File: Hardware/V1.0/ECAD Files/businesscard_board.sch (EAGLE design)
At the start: 31 parts, among them Y1 16MHz

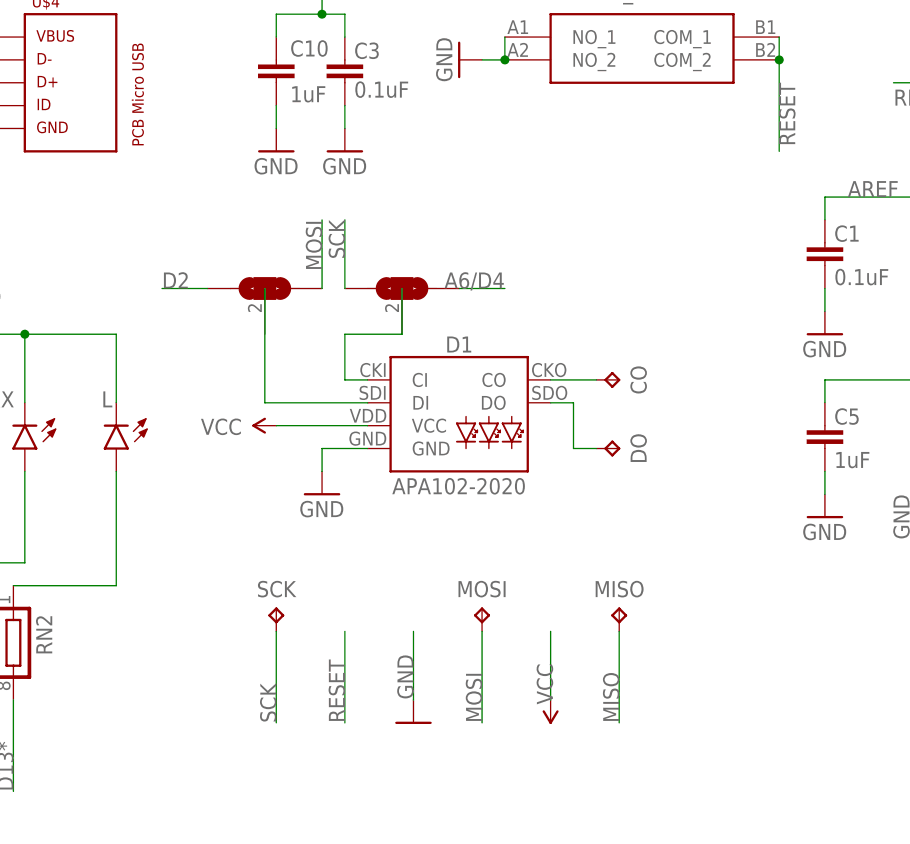
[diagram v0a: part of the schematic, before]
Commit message: Fix APA102 pinout
Fix APA102 pinout, clean up library
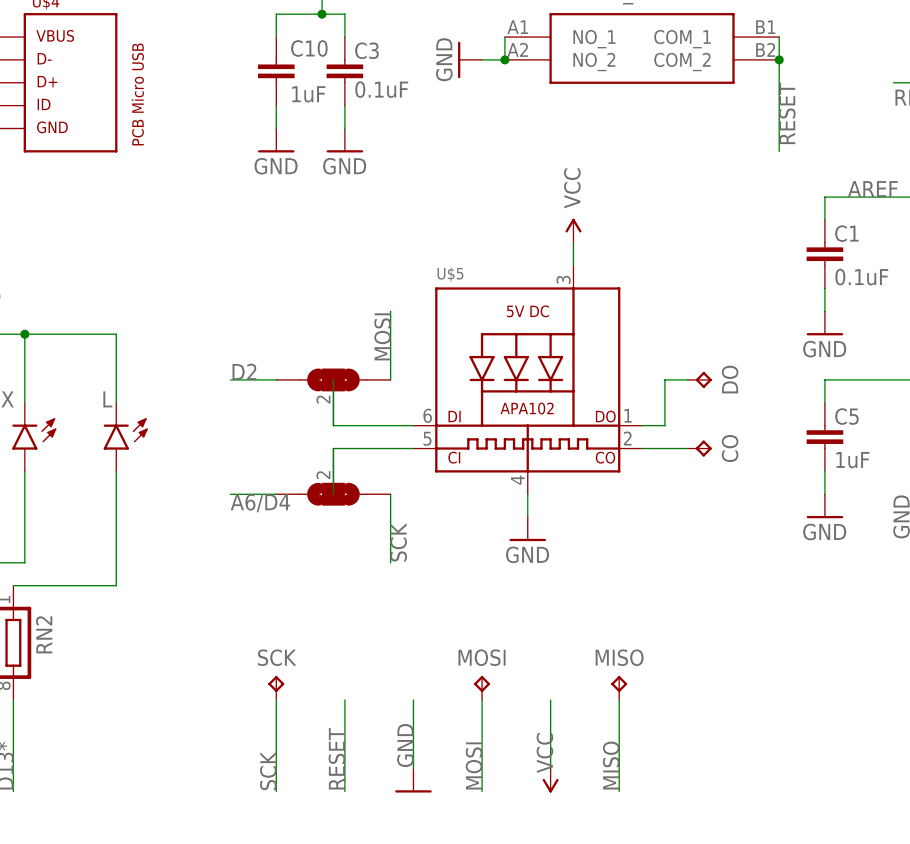
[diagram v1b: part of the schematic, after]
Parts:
- removed D1: APA102-2020, PCBusinessCard:APA102-2020
- added U$5: (no value), businesscard_board:APA1022020
- C1, C10, C2, C3, C4, C5, C6: device PCBusinessCard:CAP0603-CAP -> businesscard_board:CAP0603-CAP
- CO, DO, MISO, MOSI, SCK: device PCBusinessCard:TPTP12R -> businesscard_board:TPTP12R
- D2-/-°-MOSI, D4-/-°-SCK: device PCBusinessCard:SOLDER_JP_3WAY -> businesscard_board:SOLDER_JP_3WAY
- F1: device PCBusinessCard:PTCSMD -> businesscard_board:PTCSMD
- L, ON, RX, TX: device PCBusinessCard:LED -> businesscard_board:LED
- R2, R5, R7: device PCBusinessCard:RESISTOR0603-RES -> businesscard_board:RESISTOR0603-RES
- RN2: device PCBusinessCard:CTS742C083 -> businesscard_board:CTS742C083
- RST_SW: device PCBusinessCard:EVP-BB0AAB000 -> businesscard_board:EVP-BB0AAB000
- U$1: value ATMEGA32U4 -> 32U4; device PCBusinessCard:ATMEGA32U4 -> businesscard_board:ATMEGA32U4
- U$2: device PCBusinessCard:ARDUINO_BC -> businesscard_board:ARDUINO_BC
- U$3: device PCBusinessCard:TOUCH_SENSORS -> businesscard_board:TOUCH_SENSORS
- U$4: device PCBusinessCard:PCB_MICRO_USB_B -> businesscard_board:PCB_MICRO_USB_B
- VUSB: device PCBusinessCard:SOLDER_JP -> businesscard_board:SOLDER_JP
- Y1: device PCBusinessCard:CRYSTAL5X3 -> businesscard_board:CRYSTAL5X3
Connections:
- removed net N$7: D1.DO, DO.TP
- removed net N$8: D1.DI, D2-/-°-MOSI.MID
- removed net N$9: D1.CI, D4-/-°-SCK.MID
- new net APA102_CI: D4-/-°-SCK.MID, U$5.CKI
- new net APA102_CO: CO.TP, U$5.CKO
- new net APA102_DO: DO.TP, U$5.DO
- net GND: now also U$5.GND; no longer D1.GND
- net N$6: now also D2-/-°-MOSI.MID, U$5.DI; no longer CO.TP, D1.CO
- net VCC: now also U$5.VDD; no longer D1.VCC
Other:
- moved on the sheet: CO, DO, MISO, MOSI, SCK
